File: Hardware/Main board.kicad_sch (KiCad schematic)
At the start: 39 parts, among them J1 RBUS, U1 ESP32-S3, Y1 R940000171

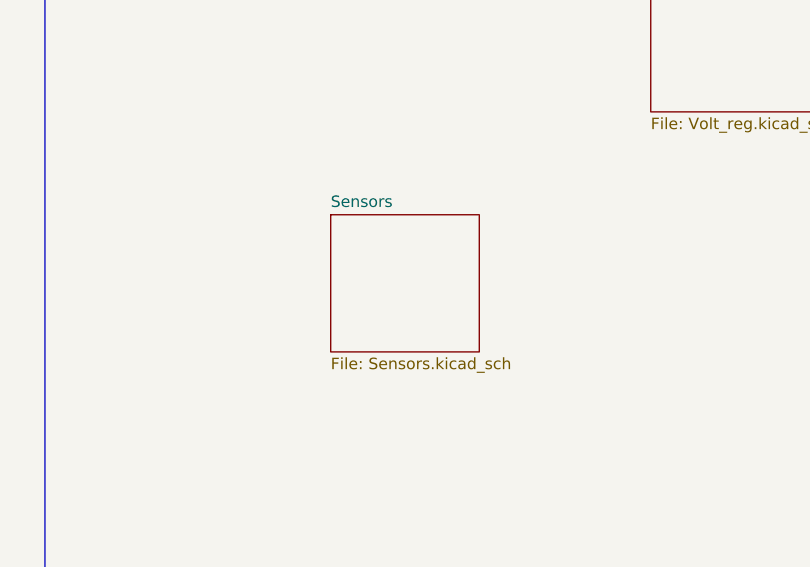
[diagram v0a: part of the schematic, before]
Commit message: Sensor completed
Barometer circuit done.
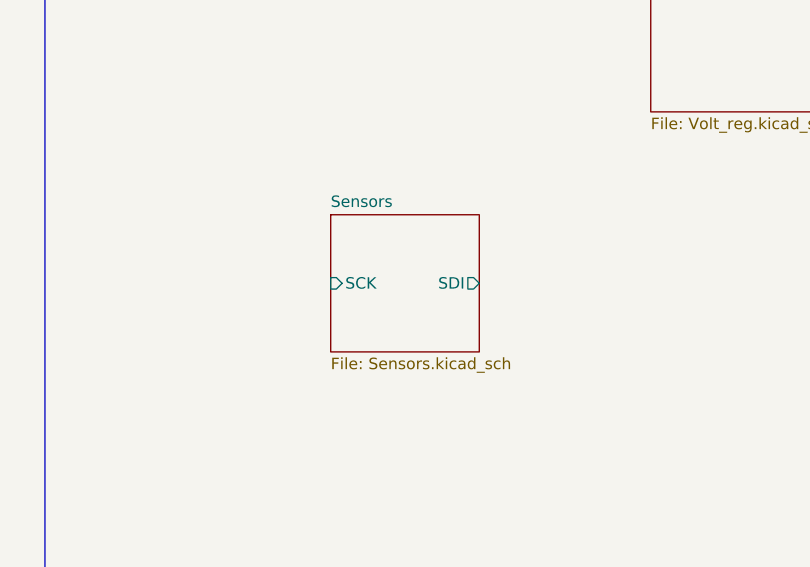
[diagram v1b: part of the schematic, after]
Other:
- sheet Sensors ports: added SCK, SDI; removed none
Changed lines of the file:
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@@
+			)
+		)
+		(pin "SDI" output
+			(at 223.52 97.79 0)
+			(effects
+				(font
+					(size 1.27 1.27)
+				)
+				(justify right)
+			)
+		)
+		(pin "SCK" input
+			(at 207.01 97.79 180)
+			(effects
+				(font
+					(size 1.27 1.27)
+				)
+				(justify left)
 			)
 		)

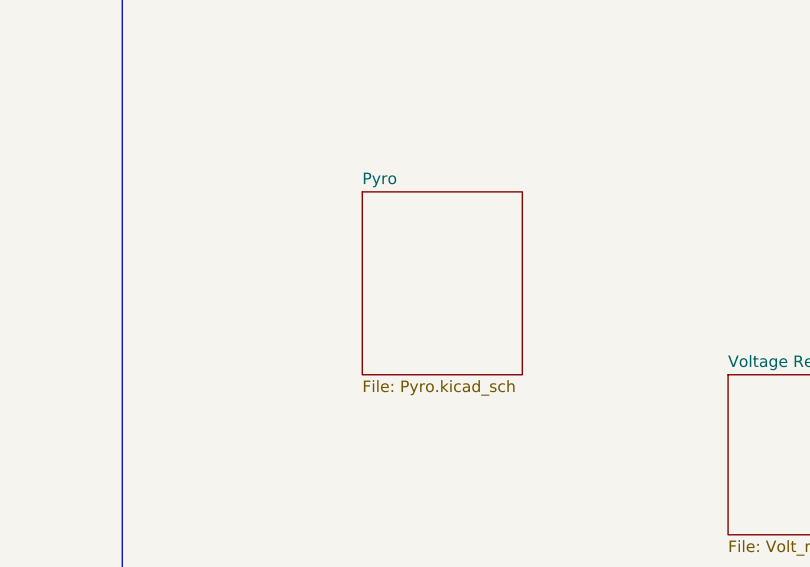
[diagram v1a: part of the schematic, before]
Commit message: Added pyro circuit
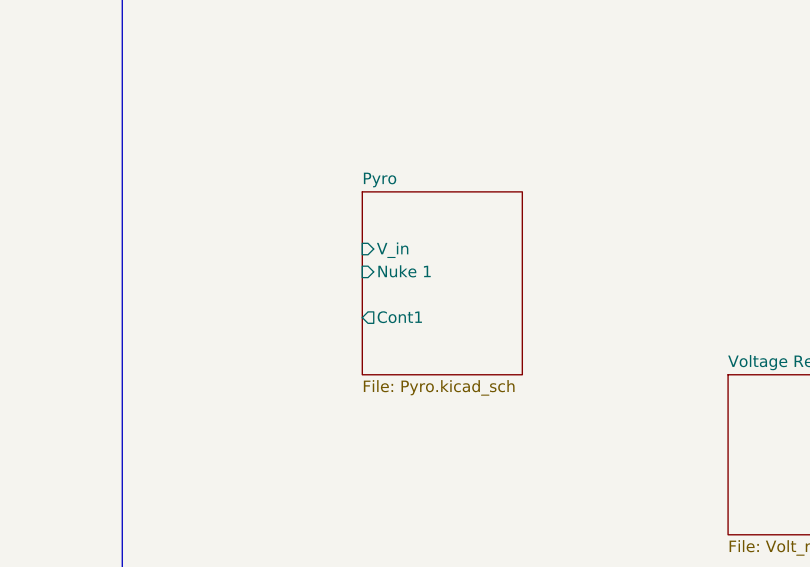
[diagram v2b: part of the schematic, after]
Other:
- sheet Pyro ports: added Cont1, Nuke 1, V_in; removed none
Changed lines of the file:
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@@
+			)
+		)
+		(pin "Cont1" output
+			(at 201.93 54.61 180)
+			(effects
+				(font
+					(size 1.27 1.27)
+				)
+				(justify left)
+			)
+		)
+		(pin "Nuke 1" input
+			(at 201.93 49.53 180)
+			(effects
+				(font
+					(size 1.27 1.27)
+				)
+				(justify left)
+			)
+		)
+		(pin "V_in" input
+			(at 201.93 46.99 180)
+			(effects
+				(font
+					(size 1.27 1.27)
+				)
+				(justify left)
 			)
 		)

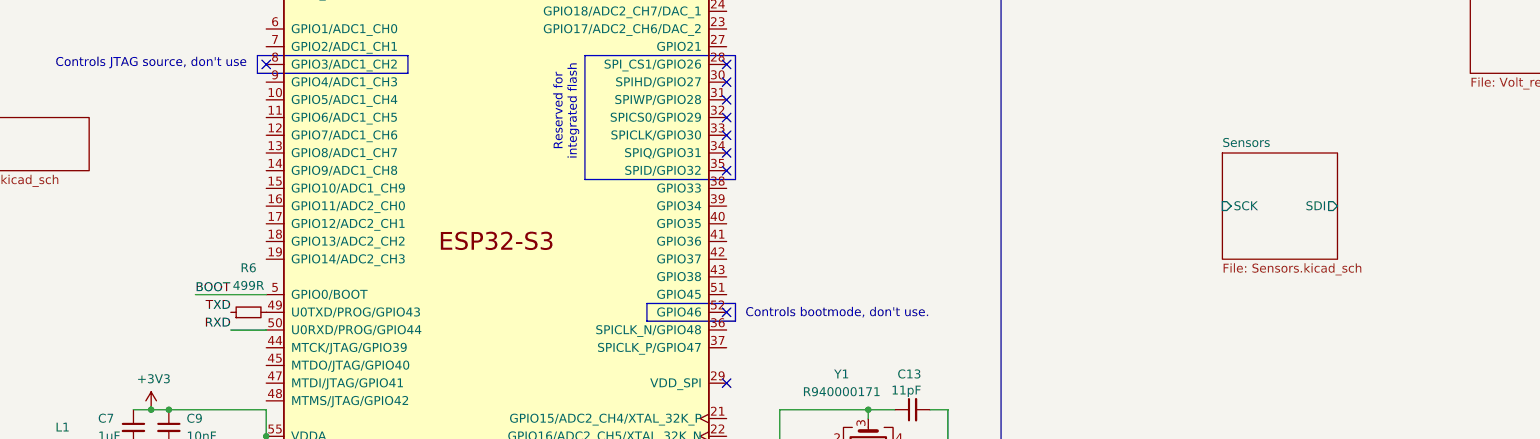
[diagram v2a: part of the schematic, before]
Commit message: Barometer sensor SPI
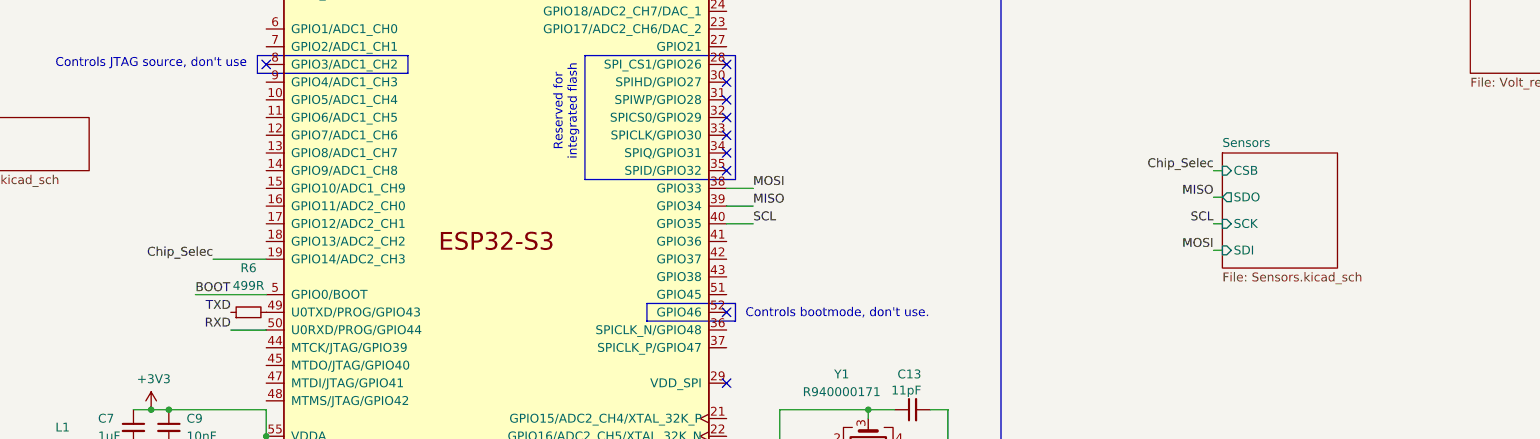
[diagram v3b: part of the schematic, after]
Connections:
- net Chip_Selec: now reaches U1.19 (GPIO14/ADC2_CH3)
- net MOSI: now reaches U1.38 (GPIO33)
- net MISO: now reaches U1.39 (GPIO34)
- net SCL: now reaches U1.40 (GPIO35)
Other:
- sheet Sensors ports: added CSB, SDO; removed none
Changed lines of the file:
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@@
 		)
 	)
+	(wire
+		(pts
+			(xy 62.23 105.41) (xy 69.85 105.41)
+		)
+		(stroke
+			(width 0)
+			(type default)
+		)
+	)
 	(polyline
 		(pts
@@
 	(wire
 		(pts
+			(xy 135.89 97.79) (xy 139.7 97.79)
+		)
+		(stroke
+			(width 0)
+			(type default)
+		)
+	)
+	(wire
+		(pts
 			(xy 64.77 115.57) (xy 69.85 115.57)
 		)
@@
 		)
 	)
+	(wire
+		(pts
+			(xy 135.89 95.25) (xy 139.7 95.25)
+		)
+		(stroke
+			(width 0)
+			(type default)
+		)
+	)
 	(polyline
 		(pts
@@
 	(wire
 		(pts
+			(xy 205.74 104.14) (xy 207.01 104.14)
+		)
+		(stroke
+			(width 0)
+			(type default)
+		)
+	)
+	(wire
+		(pts
 			(xy 27.94 40.64) (xy 30.48 40.64)
 		)
@@
 	(wire
 		(pts
+			(xy 205.74 100.33) (xy 207.01 100.33)
+		)
+		(stroke
+			(width 0)
+			(type default)
+		)
+	)
+	(wire
+		(pts
 			(xy 278.13 33.02) (xy 273.05 33.02)
 		)
@@
 	(wire
 		(pts
+			(xy 205.74 92.71) (xy 207.01 92.71)
+		)
+		(stroke
+			(width 0)
+			(type default)
+		)
+	)
+	(wire
+		(pts
 			(xy 148.59 132.08) (xy 151.13 132.08)
 		)
@@
 	(wire
 		(pts
+			(xy 135.89 100.33) (xy 139.7 100.33)
+		)
+		(stroke
+			(width 0)
+			(type default)
+		)
+	)
+	(wire
+		(pts
 			(xy 39.37 21.59) (xy 44.45 21.59)
 		)
@@
 	(wire
 		(pts
+			(xy 205.74 96.52) (xy 207.01 96.52)
+		)
+		(stroke
+			(width 0)
+			(type default)
+		)
+	)
+	(wire
+		(pts
 			(xy 73.66 26.67) (xy 71.12 26.67)
 		)
@@
 		)
 	)
+	(label "Chip_Selec"
+		(at 205.74 92.71 180)
+		(fields_autoplaced yes)
+		(effects
+			(font
+				(size 1.27 1.27)
+			)
+			(justify right bottom)
+		)
+	)
 	(label "CHIP_PU"
 		(at 36.83 165.1 180)
@@
 		)
 	)
+	(label "MISO"
+		(at 139.7 97.79 0)
+		(fields_autoplaced yes)
+		(effects
+			(font
+				(size 1.27 1.27)
+			)
+			(justify left bottom)
+		)
+	)
+	(label "MOSI"
+		(at 139.7 95.25 0)
+		(fields_autoplaced yes)
+		(effects
+			(font
+				(size 1.27 1.27)
+			)
+			(justify left bottom)
+		)
+	)
 	(label "CAN+"
 		(at 115.57 185.42 0)
@@
 		)
 	)
+	(label "MISO"
+		(at 205.74 96.52 180)
+		(fields_autoplaced yes)
+		(effects
+			(font
+				(size 1.27 1.27)
+			)
+			(justify right bottom)
+		)
+	)
 	(label "CAN_RX"
 		(at 13.97 40.64 0)
@@
 		)
 	)
+	(label "SCL"
+		(at 139.7 100.33 0)
+		(fields_autoplaced yes)
+		(effects
+			(font
+				(size 1.27 1.27)
+			)
+			(justify left bottom)
+		)
+	)
 	(label "RXD"
 		(at 64.77 115.57 180)
@@
 		)
 	)
+	(label "Chip_Selec"
+		(at 62.23 105.41 180)
+		(fields_autoplaced yes)
+		(effects
+			(font
+				(size 1.27 1.27)
+			)
+			(justify right bottom)
+		)
+	)
+	(label "SCL"
+		(at 205.74 100.33 180)
+		(fields_autoplaced yes)
+		(effects
+			(font
+				(size 1.27 1.27)
+			)
+			(justify right bottom)
+		)
+	)
+	(label "MOSI"
+		(at 205.74 104.14 180)
+		(fields_autoplaced yes)
+		(effects
+			(font
+				(size 1.27 1.27)
+			)
+			(justify right bottom)
+		)
+	)
 	(label "CAN_RX"
 		(at 115.57 182.88 0)
@@
 	(sheet
 		(at 207.01 90.17)
-		(size 16.51 15.24)
+		(size 16.51 16.51)
 		(fields_autoplaced yes)
 		(stroke
@@
 		)
 		(property "Sheetfile" "Sensors.kicad_sch"
-			(at 207.01 105.9946 0)
+			(at 207.01 107.2646 0)
 			(effects
 				(font
@@
 			)
 		)
-		(pin "SDI" output
-			(at 223.52 97.79 0)
+		(pin "SDI" input
+			(at 207.01 104.14 180)
 			(effects
 				(font
 					(size 1.27 1.27)
 				)
-				(justify right)
+				(justify left)
 			)
 		)
 		(pin "SCK" input
-			(at 207.01 97.79 180)
+			(at 207.01 100.33 180)
+			(effects
+				(font
+					(size 1.27 1.27)
+				)
+				(justify left)
+			)
+		)
+		(pin "SDO" output
+			(at 207.01 96.52 180)
+			(effects
+				(font
+					(size 1.27 1.27)
+				)
+				(justify left)
+			)
+		)
+		(pin "CSB" input
+			(at 207.01 92.71 180)
 			(effects
 				(font

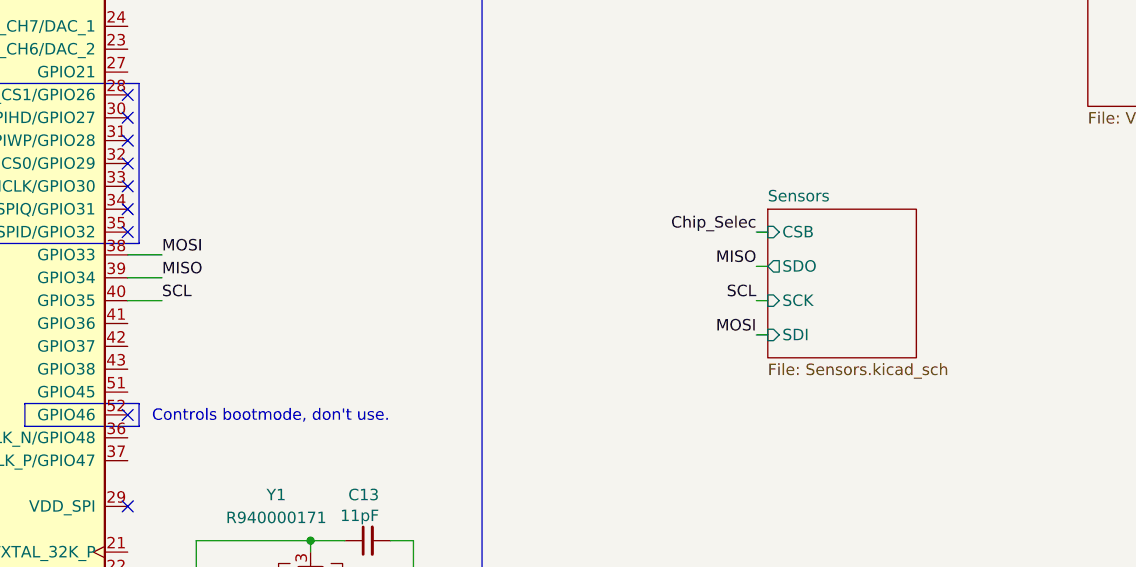
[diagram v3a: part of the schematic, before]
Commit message: Barometer fix + Photo sensor
Fixed orientation of ground for barometer. Added Photo sensor + photo sensor symbol in library.

Need to determine resistance for photo sensor circuit.
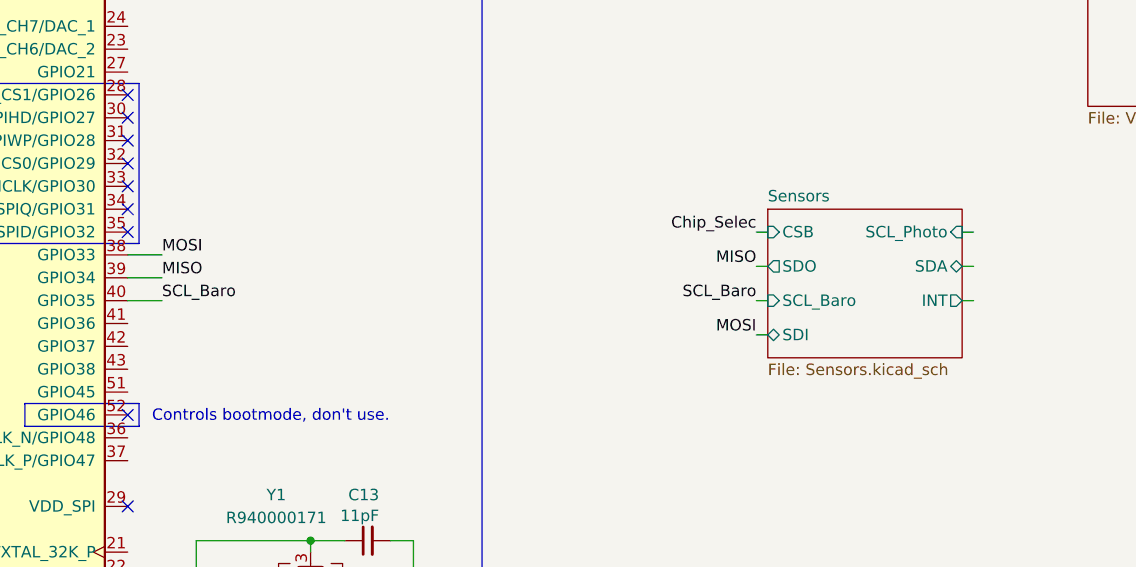
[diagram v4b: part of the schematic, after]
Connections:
- net SCL renamed SCL_Baro
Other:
- sheet Sensors ports: added INT, SCL_Baro, SCL_Photo, SDA; removed SCK
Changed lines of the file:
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@@
 	(wire
 		(pts
+			(xy 228.6 96.52) (xy 229.87 96.52)
+		)
+		(stroke
+			(width 0)
+			(type default)
+		)
+	)
+	(wire
+		(pts
 			(xy 30.48 191.77) (xy 30.48 190.5)
 		)
@@
 	(wire
 		(pts
+			(xy 228.6 100.33) (xy 229.87 100.33)
+		)
+		(stroke
+			(width 0)
+			(type default)
+		)
+	)
+	(wire
+		(pts
 			(xy 16.51 170.18) (xy 16.51 171.45)
 		)
@@
 		)
 	)
+	(wire
+		(pts
+			(xy 228.6 92.71) (xy 229.87 92.71)
+		)
+		(stroke
+			(width 0)
+			(type default)
+		)
+	)
 	(polyline
 		(pts
@@
 		)
 	)
+	(label "SCL_Baro"
+		(at 205.74 100.33 180)
+		(fields_autoplaced yes)
+		(effects
+			(font
+				(size 1.27 1.27)
+			)
+			(justify right bottom)
+		)
+	)
 	(label "Data-"
 		(at 99.06 162.56 0)
@@
 		)
 	)
-	(label "SCL"
+	(label "SCL_Baro"
 		(at 139.7 100.33 0)
 		(fields_autoplaced yes)
@@
 		)
 	)
-	(label "SCL"
-		(at 205.74 100.33 180)
-		(fields_autoplaced yes)
-		(effects
-			(font
-				(size 1.27 1.27)
-			)
-			(justify right bottom)
-		)
-	)
 	(label "MOSI"
 		(at 205.74 104.14 180)
@@
 	(sheet
 		(at 207.01 90.17)
-		(size 16.51 16.51)
+		(size 21.59 16.51)
 		(fields_autoplaced yes)
 		(stroke
@@
 			)
 		)
-		(pin "SDI" input
-			(at 207.01 104.14 180)
+		(pin "SDO" output
+			(at 207.01 96.52 180)
 			(effects
 				(font
@@
 			)
 		)
-		(pin "SCK" input
-			(at 207.01 100.33 180)
+		(pin "CSB" input
+			(at 207.01 92.71 180)
 			(effects
 				(font
@@
 			)
 		)
-		(pin "SDO" output
-			(at 207.01 96.52 180)
+		(pin "SDA" bidirectional
+			(at 228.6 96.52 0)
+			(effects
+				(font
+					(size 1.27 1.27)
+				)
+				(justify right)
+			)
+		)
+		(pin "INT" output
+			(at 228.6 100.33 0)
+			(effects
+				(font
+					(size 1.27 1.27)
+				)
+				(justify right)
+			)
+		)
+		(pin "SCL_Baro" input
+			(at 207.01 100.33 180)
 			(effects
 				(font
@@
 			)
 		)
-		(pin "CSB" input
-			(at 207.01 92.71 180)
+		(pin "SCL_Photo" input
+			(at 228.6 92.71 0)
+			(effects
+				(font
+					(size 1.27 1.27)
+				)
+				(justify right)
+			)
+		)
+		(pin "SDI" bidirectional
+			(at 207.01 104.14 180)
 			(effects
 				(font

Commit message: USB-C + Voltage stuff
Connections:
- net CAN_RX: now also U1.23 (GPIO17/ADC2_CH6/DAC_2)
- net CAN_TX: now also U1.24 (GPIO18/ADC2_CH7/DAC_1)
- net SDA-Photo: now reaches U1.17 (GPIO12/ADC2_CH1)
- net SDA-CS: now reaches U1.18 (GPIO13/ADC2_CH2)
- net Nuke 1: now reaches U1.41 (GPIO36)
- net Cont 1: now reaches U1.42 (GPIO37)
- net SCL_I2C: now reaches U1.43 (GPIO38)
- net SCL_Baro renamed SCK_Baro
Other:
- added sheet USB-RBUS (USB-RBUS.kicad_sch)
- sheet Sensors ports: added SDA_Photo; removed SDA
- sheet Voltage Regulation ports: added BUS_VMON, EN, SCL, SDA-CurrentSens, VIN; removed none
